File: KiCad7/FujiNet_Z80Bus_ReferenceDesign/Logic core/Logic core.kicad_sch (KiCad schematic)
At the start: 13 parts, among them IC1 74HC32N, IC2 7404N, IC3 7474N, IC4 74HC08N

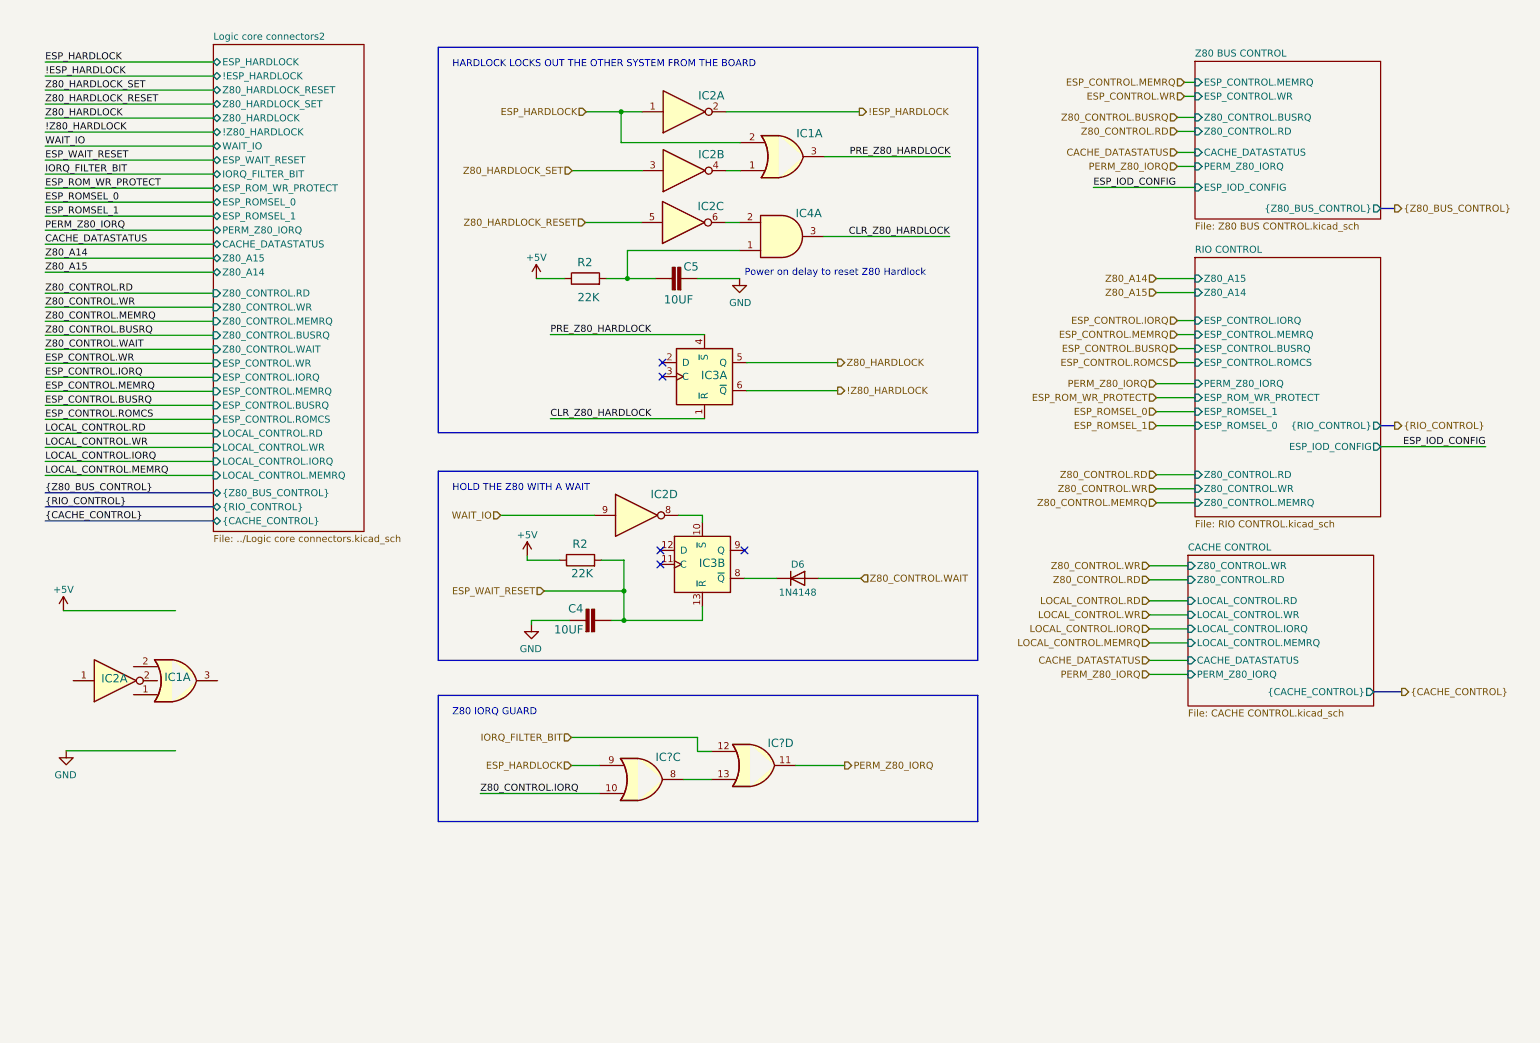
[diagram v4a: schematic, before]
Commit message: KiCAD - grid alignment errors fixed
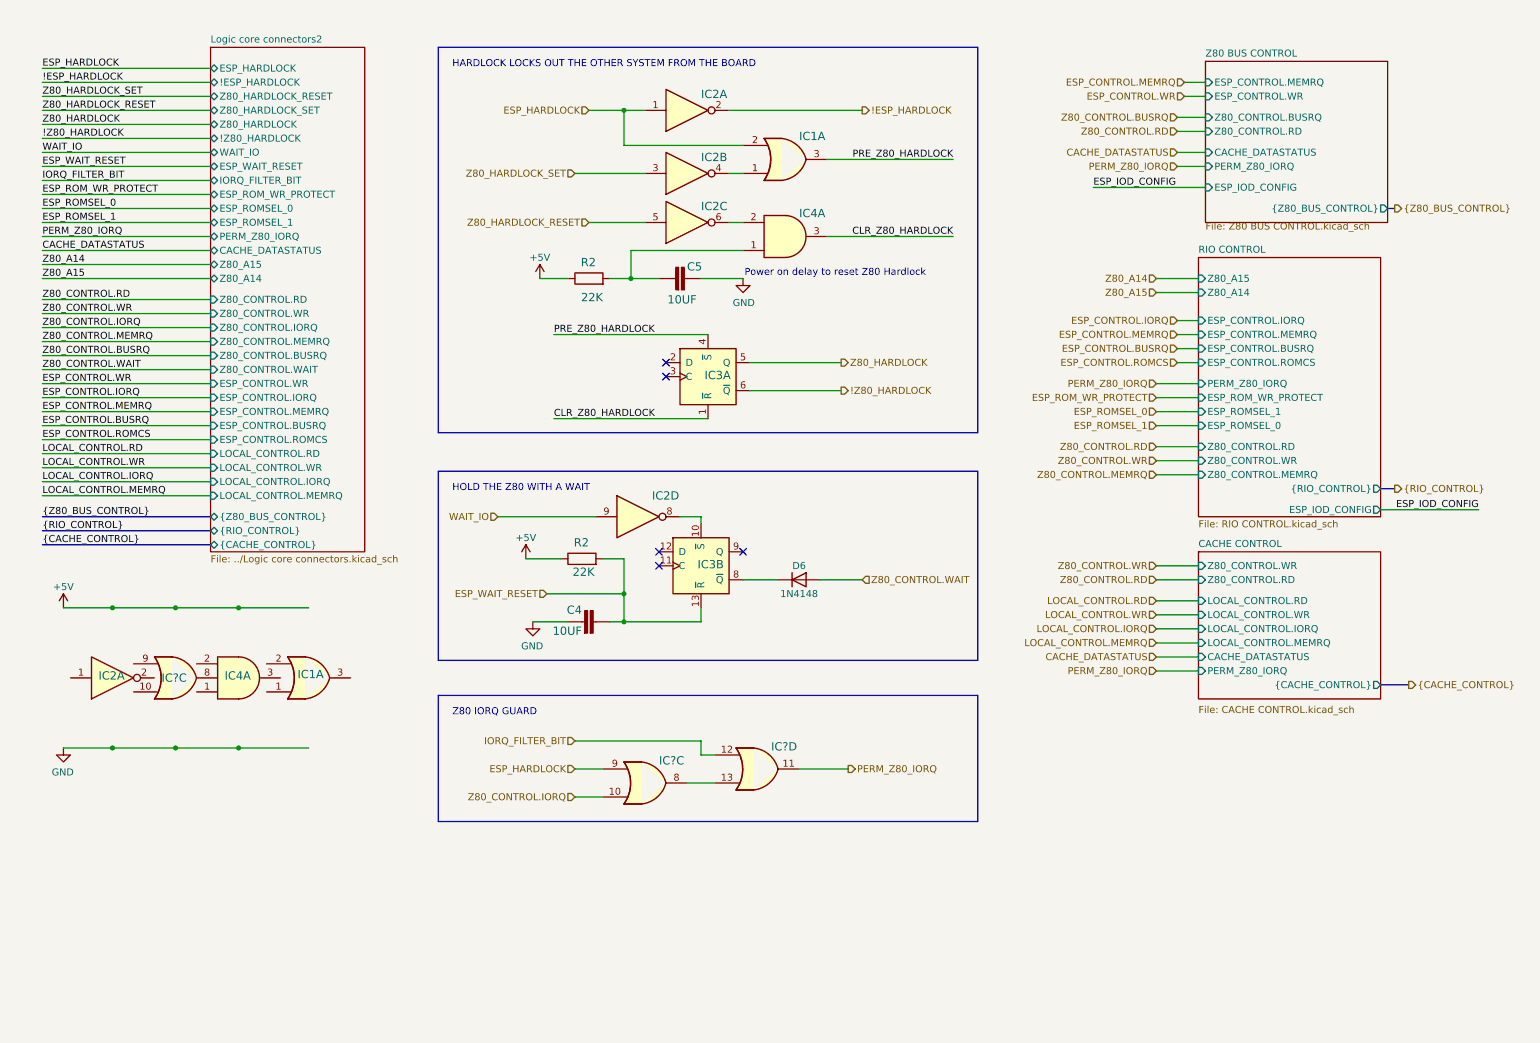
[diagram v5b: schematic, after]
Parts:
- added IC4: 74HC08N, Package_DIP:DIP-14_W7.62mm_Socket, symbol 74xx:74LS08
- added IC?: 74HC32N, Package_DIP:DIP-14_W7.62mm_Socket, symbol 74xx:74LS32
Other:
- sheet Logic core connectors2 ports: added Z80_CONTROL.IORQ; removed none
- moved on the sheet: C5, IC1A, IC2A, IC2B, IC2C, IC3A, IC4A, IC?C, IC?D, R2

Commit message: Kicad Symbols error fixes and ERC bug fixes
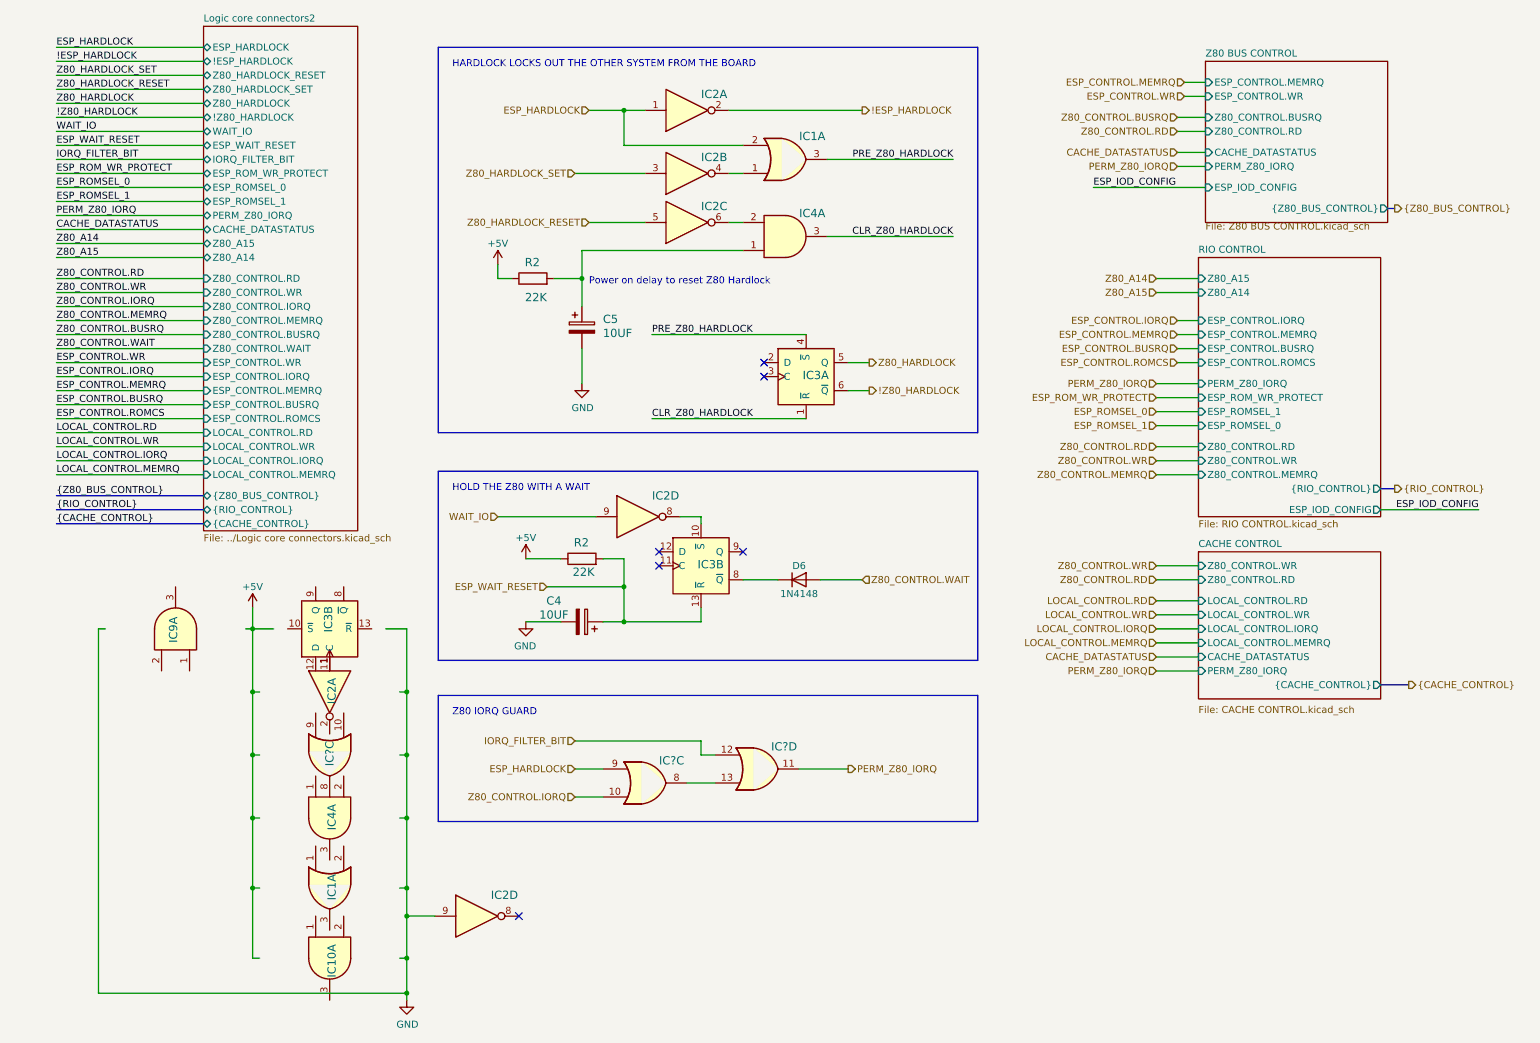
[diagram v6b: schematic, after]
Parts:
- added IC10, IC9: 74HC08N, Package_DIP:DIP-14_W7.62mm_Socket, symbol 74xx:74LS08
- added IC2: 7404N, Package_DIP:DIP-14_W7.62mm_Socket, symbol 74xx:74HC04
- added IC3: 7474N, Package_DIP:DIP-14_W7.62mm_Socket, symbol 74xx:74HC74
- C4, C5: symbol FujiNet_Z80Bus_Reference-rescue:C-EU050-050X075-Z80ESP-eagle-import -> Device:C_Polarized
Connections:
- net GND: now also IC2.9
- no-connect marks 5 -> 6
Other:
- moved on the sheet: IC1A, IC2A, IC3A, IC4A, IC?C, R2

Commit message: KiCad - ALMOST ERROR FREE!!!!
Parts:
- added IC1 (x5), IC7, IC8: 74HC32N, Package_DIP:DIP-14_W7.62mm_Socket, symbol 74xx:74LS32
- added IC4 (x2): 74HC08N, Package_DIP:DIP-14_W7.62mm_Socket, symbol 74xx:74LS08
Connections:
- net GND: now also IC1.1, IC1.1, IC1.1, IC1.1, IC1.2, IC1.2, IC1.2, IC1.2, IC4.1, IC4.1, IC4.2, IC4.2
- no-connect marks 6 -> 12
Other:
- moved on the sheet: IC2D
